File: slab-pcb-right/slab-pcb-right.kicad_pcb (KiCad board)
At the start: 2 copper layers, 158 x 104 mm, 140 parts, among them J1 Conn_01x04, J2 Conn_01x04, J3 TRRS_L, J4 TRRS_R, J5 SSD1306, SW1 RotaryEncoder, U1 Seeeduino Xiao rp2040, U2 PCA9555PW, U3 PCA9555PW, U4 ADS1110, U5 SN74AHCT125PWR, U6 TCA4307DGKR

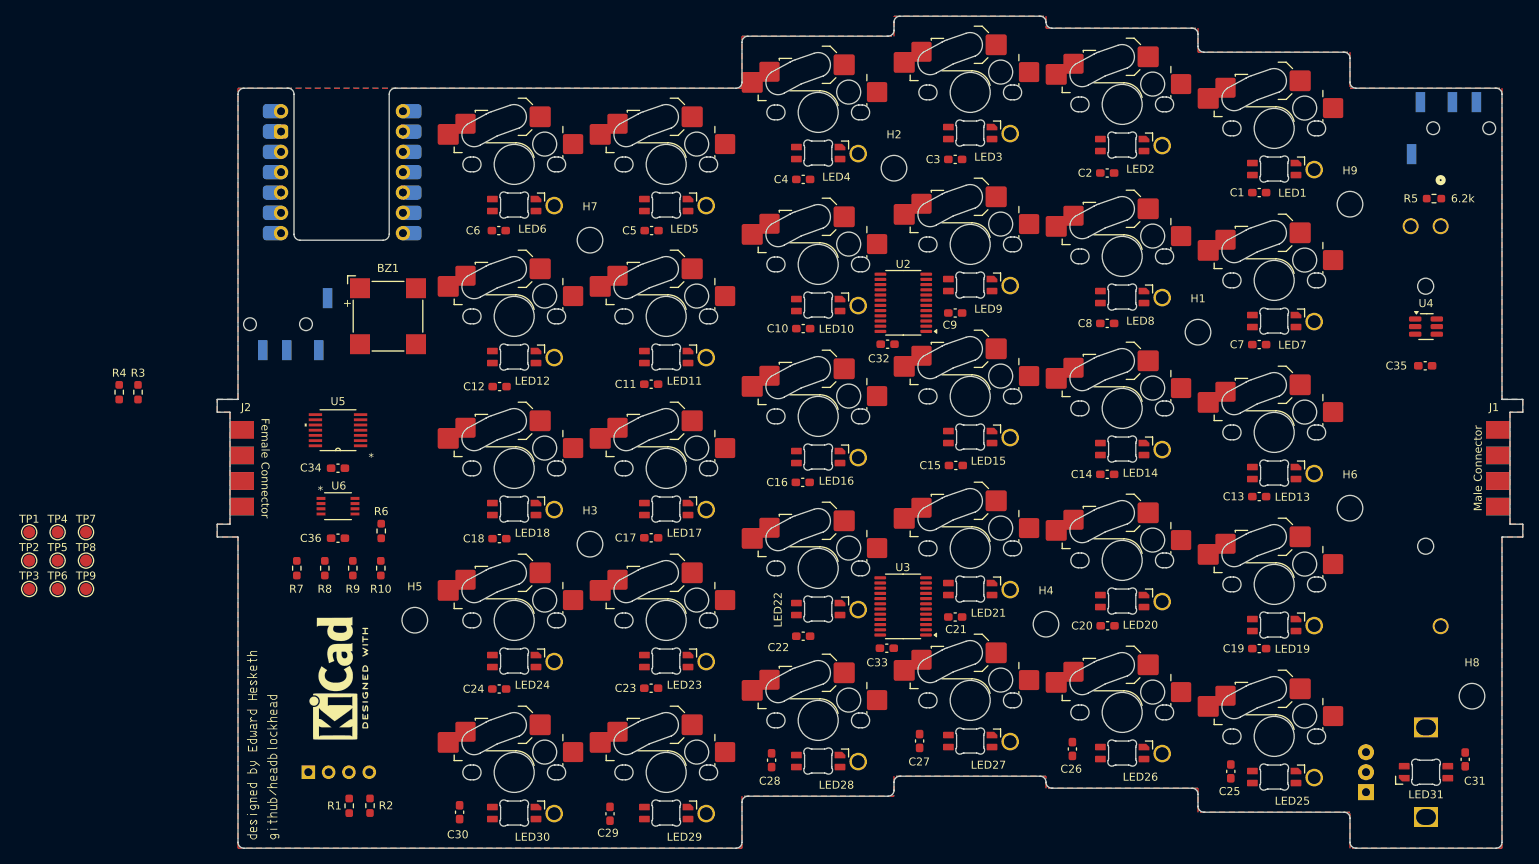
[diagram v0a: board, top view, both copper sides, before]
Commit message: feat: route keys of slab-right
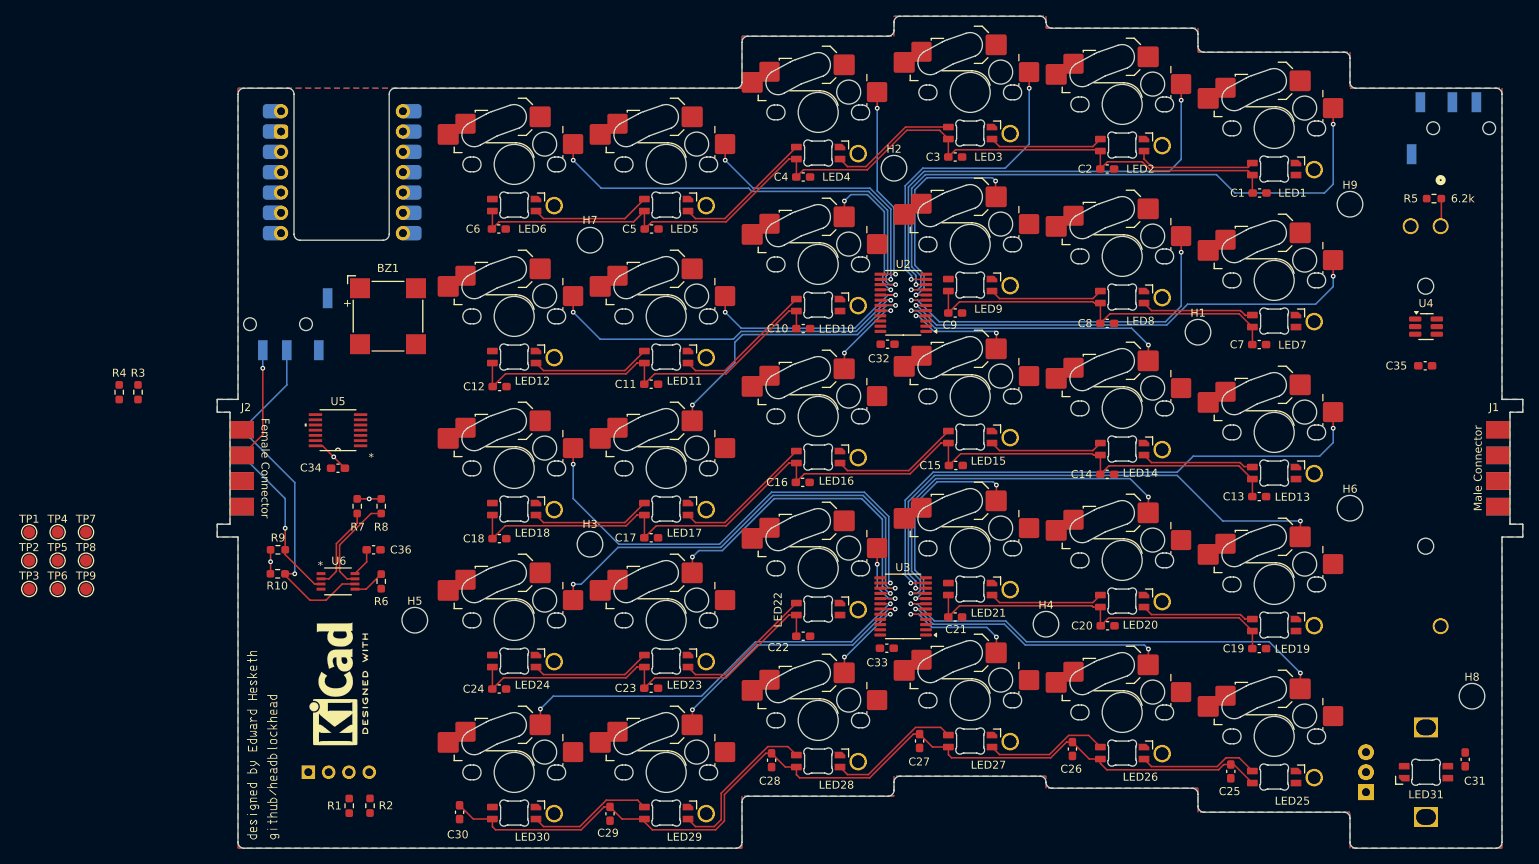
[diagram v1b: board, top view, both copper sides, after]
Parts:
- moved R10 12.9 mm to (75.0, 115.7), turned to 180 degrees
- moved R7 10.8 mm to (84.9, 107.2), turned to -90 degrees
- moved R8 10.5 mm to (87.9, 107.2), turned to -90 degrees
- moved R9 9.64 mm to (75.0, 112.7), turned to 180 degrees
- moved U6 9.40 mm to (82.5, 116.7)
- moved R6 6.30 mm to (87.9, 116.7)
- moved C36 4.68 mm to (87.0, 112.7), turned to 180 degrees
- moved REF** 0.70 mm to (81.9, 129.5)
- moved C2 0.50 mm to (178.7, 65.1)
- moved C4 0.30 mm to (140.7, 66.1)
- moved C3 0.30 mm to (159.7, 63.6)
- moved C5 0.20 mm to (121.7, 72.6)
- moved C6 0.20 mm to (102.6, 72.6)
- moved C1 0.07 mm to (197.7, 68.1)
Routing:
- net VBUS: track 0.00 -> 552.4 mm
- net /KEY1: track 0.00 -> 80.3 mm, vias 0 -> 2
- net /KEY13: track 0.00 -> 72.8 mm, vias 0 -> 2
- net /KEY19: track 0.00 -> 67.2 mm, vias 0 -> 2
- net /KEY18: track 0.00 -> 61.7 mm, vias 0 -> 2
- net /KEY7: track 0.00 -> 59.8 mm, vias 0 -> 2
- net /KEY2: track 0.00 -> 58.8 mm, vias 0 -> 2
- net /KEY24: track 0.00 -> 58.5 mm, vias 0 -> 2
- net /KEY25: track 0.00 -> 56.2 mm, vias 0 -> 2
- net /KEY6: track 0.00 -> 56.1 mm, vias 0 -> 2
- net /KEY30: track 0.00 -> 52.5 mm, vias 0 -> 2
- net /KEY20: track 0.00 -> 48.4 mm, vias 0 -> 2
- net /KEY12: track 0.00 -> 46.4 mm, vias 0 -> 2
- net /KEY8: track 0.00 -> 46.3 mm, vias 0 -> 2
- net /I2C_BUS_SDA: track 0.00 -> 45.3 mm, vias 0 -> 1
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
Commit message: feat: finish routing slab-pcb-right
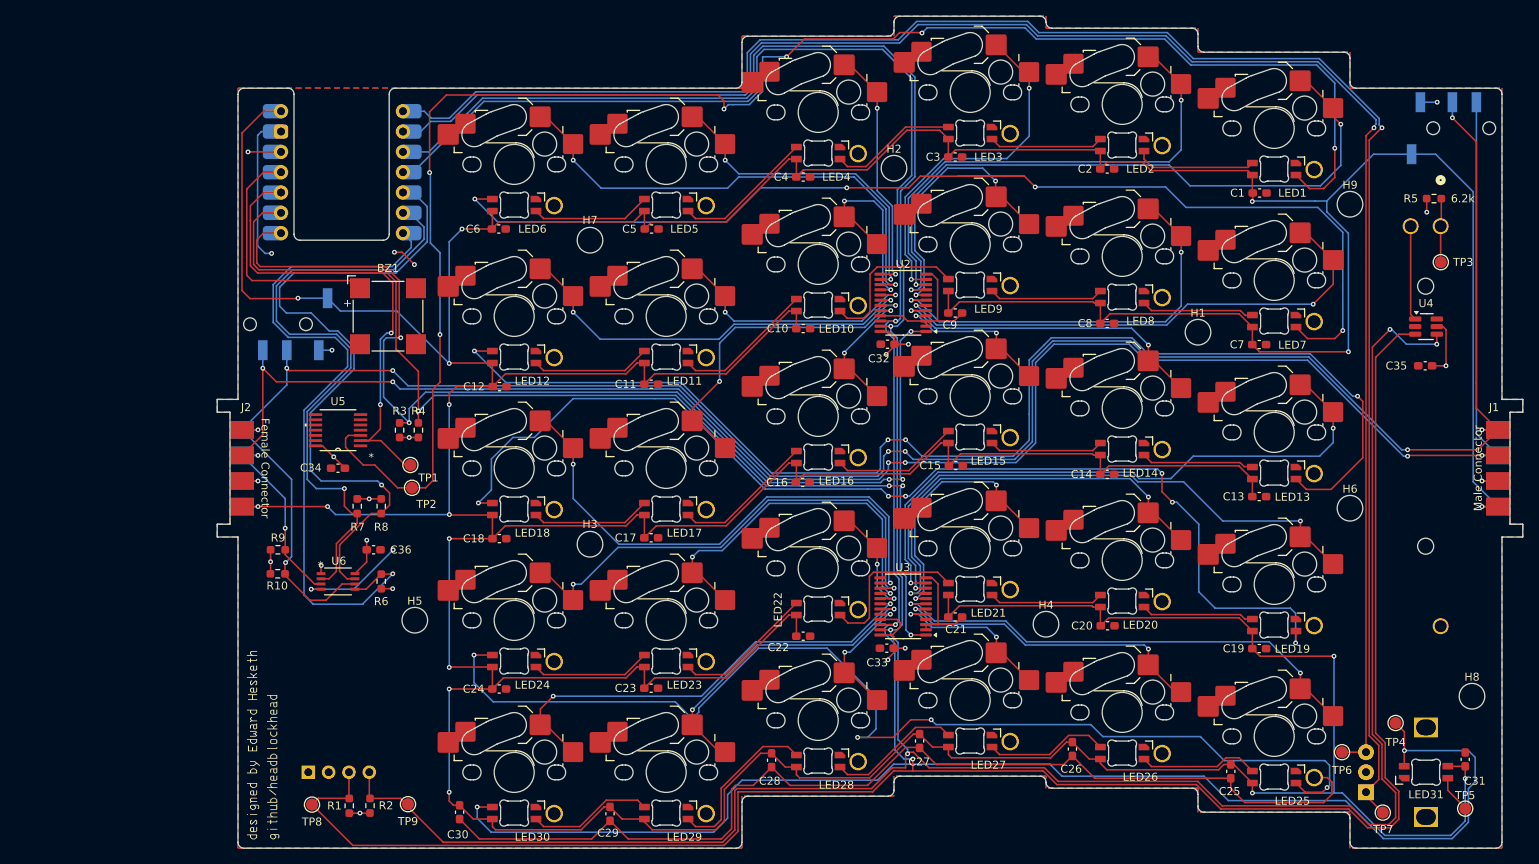
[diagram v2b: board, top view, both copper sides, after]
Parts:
- removed REF**: KiCad-Logo2_6mm_SilkScreen, Symbol:KiCad-Logo2_6mm_SilkScreen
- moved TP3 181.1 mm to (220.3, 76.8)
- moved TP5 178.7 mm to (223.4, 145.1)
- moved TP4 168.9 mm to (214.7, 134.3)
- moved TP7 165.8 mm to (213.1, 145.6)
- moved TP6 161.8 mm to (208.0, 138.0)
- moved TP2 48.7 mm to (91.8, 105.0)
- moved TP9 48.4 mm to (91.2, 144.5)
- moved TP1 48.4 mm to (91.5, 102.1)
- moved TP8 41.6 mm to (79.2, 144.6)
- moved R4 37.7 mm to (92.5, 97.8)
- moved R3 33.0 mm to (90.2, 97.8)
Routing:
- net /I2C0_SCL: track 0.00 -> 392.1 mm, vias 0 -> 3
- net /I2C0_SDA: track 0.00 -> 383.4 mm, vias 0 -> 5
- net VBUS: track 552.4 -> 914.9 mm, vias 0 -> 17
- net /I2C_BUS_SCL: track 34.9 -> 265.6 mm, vias 2 -> 8
- net /I2C_BUS_SDA: track 45.3 -> 274.0 mm, vias 1 -> 9
- net /ROT_A: track 0.00 -> 223.8 mm, vias 0 -> 1
- net /ROT_B: track 0.00 -> 217.3 mm, vias 0 -> 1
- net GND: track 0.00 -> 206.5 mm, vias 0 -> 7
- net /SHIFTER_OUTPUT: track 0.00 -> 206.5 mm, vias 0 -> 6
- net /RGBLEDARRAY_OUTPUT: track 0.00 -> 161.4 mm, vias 0 -> 2
- net Net-(LED12-DOUT): track 0.00 -> 156.6 mm, vias 0 -> 4
- net Net-(LED6-DOUT): track 0.00 -> 144.5 mm, vias 0 -> 4
- net Net-(LED24-DOUT): track 0.00 -> 140.5 mm, vias 0 -> 4
- net /EXPANDER1_INT: track 0.00 -> 137.7 mm, vias 0 -> 5
- net Net-(LED18-DOUT): track 0.00 -> 137.1 mm, vias 0 -> 6
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
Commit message: feat: finialise slab-pcb-right
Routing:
- net Net-(LED6-DOUT): track 144.5 -> 136.2 mm
- net Net-(LED12-DOUT): track 156.6 -> 154.7 mm
- net /I2C_BUS_SDA: track 274.0 -> 272.9 mm
- net /EXPANDER1_INT: track 137.7 -> 138.3 mm
- net /EXPANDER2_INT: track 134.0 -> 134.6 mm
